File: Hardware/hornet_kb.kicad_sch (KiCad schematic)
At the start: 33 parts, among them J1 Conn_ST_STDC14, J10 USB_C_Receptacle_USB2.0, SW98 SW_Push, U1 nRF52840, Y1 32.768kHz, Y3 Crystal_GND24

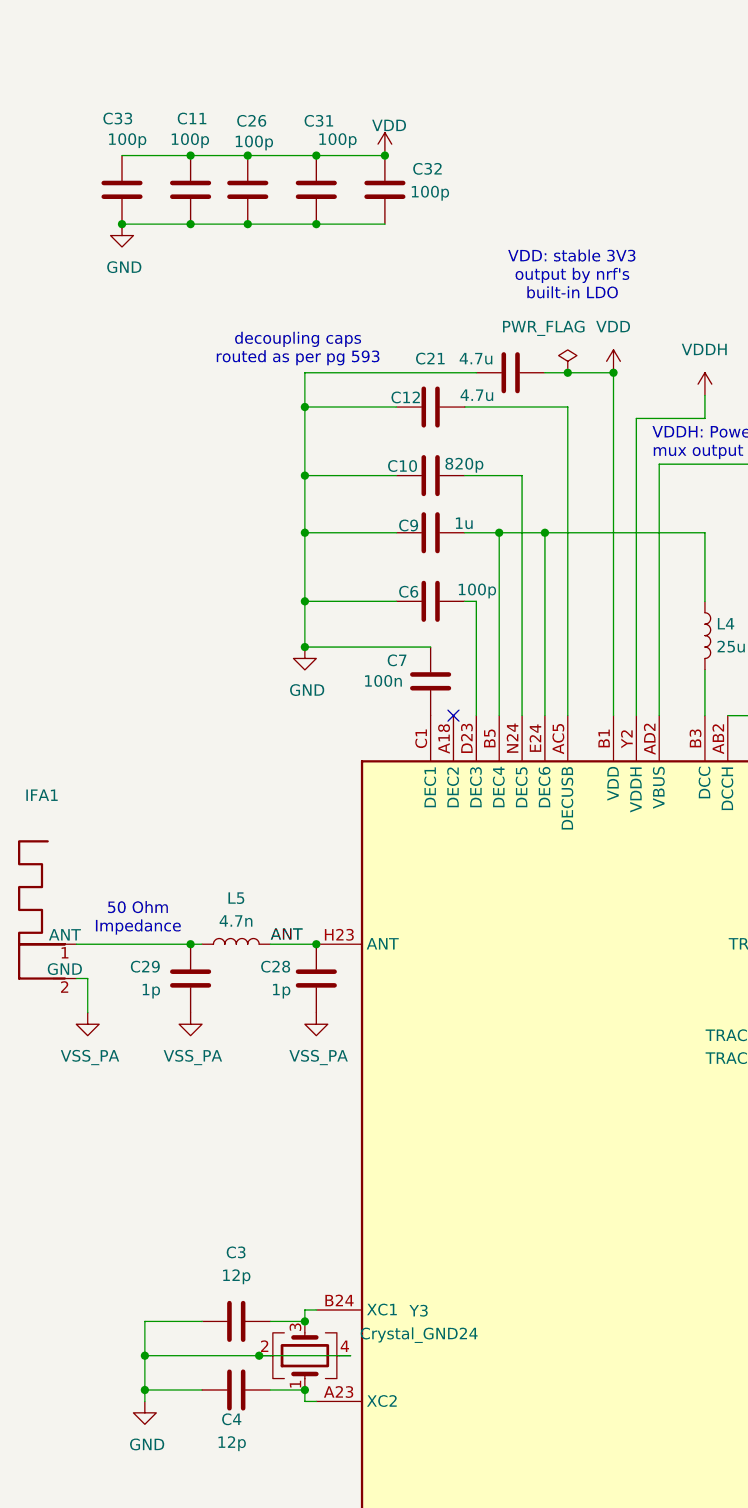
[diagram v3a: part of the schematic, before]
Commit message: Add LCSC part numbers and new resistor to PCB
Added LCSC part numbers to multiple components in hornet_kb.kicad_pcb for improved BOM generation. Introduced a new 500Ω resistor (R11) and updated net assignments for Q1 and D27. Modified .gitignore to exclude backup and auto-save files, and removed obsolete backup files from Hardware/hornet_kb-backups. Made symbol and footprint tweaks in Custom_sym.kicad_sym.
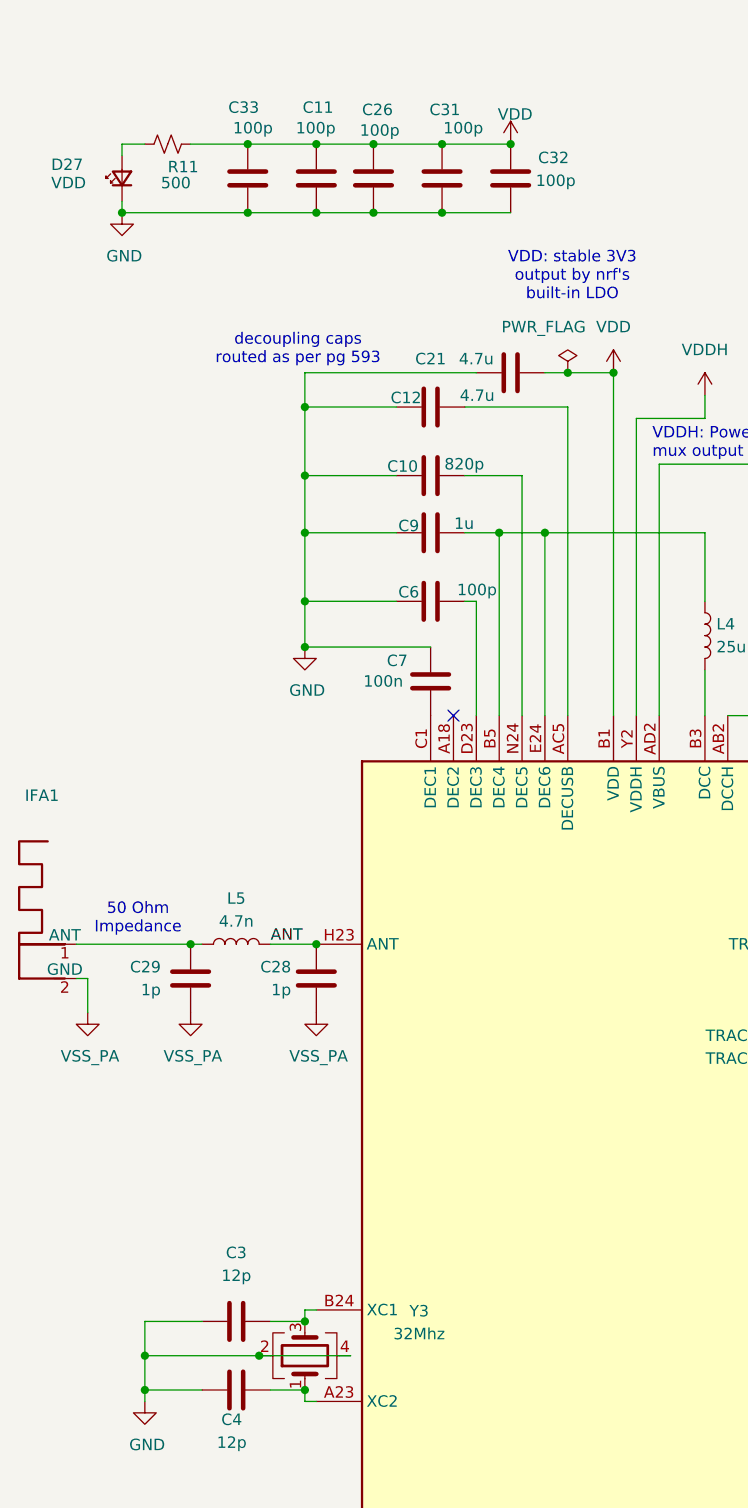
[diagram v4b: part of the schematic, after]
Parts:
- added D27: VDD, LED_SMD:LED_0402_1005Metric, symbol Device:LED_Small
- added R11: 500, Resistor_SMD:R_0603_1608Metric, symbol Device:R_Small_US
- J1: now left out of the parts list
- R23, R24: LCSC C23186 -> (none)
- R7: LCSC C23345 -> (none)
- Y1: LCSC (none) -> C32346
- Y3: value Crystal_GND24 -> 32Mhz; LCSC (none) -> C5339095
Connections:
- net GND: now also D27.1 (K)
- net VDD: now also R11.1
- new net: D27.2 (A), R11.2
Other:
- moved on the sheet: C11, C26, C31, C32, C33

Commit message: Added LCSC part defs
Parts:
- C1, C2, C3, C4: LCSC (none) -> C1547
- C10: LCSC (none) -> C107057
- C11, C26, C31, C32, C33, C6: LCSC (none) -> C14858
- C12, C21, C5: LCSC (none) -> C1779
- C28, C29: LCSC (none) -> C1550
- C7: LCSC (none) -> C14663
- C9: LCSC (none) -> C15849
- L3: LCSC (none) -> C436512
- L4: LCSC (none) -> C12669
- L5: LCSC (none) -> C86065
- R11: LCSC (none) -> C6207671
- R12: LCSC (none) -> C25804
- R23, R24: LCSC (none) -> C23186
- R7: LCSC (none) -> C22843
